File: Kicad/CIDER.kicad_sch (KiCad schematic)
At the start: 0 parts

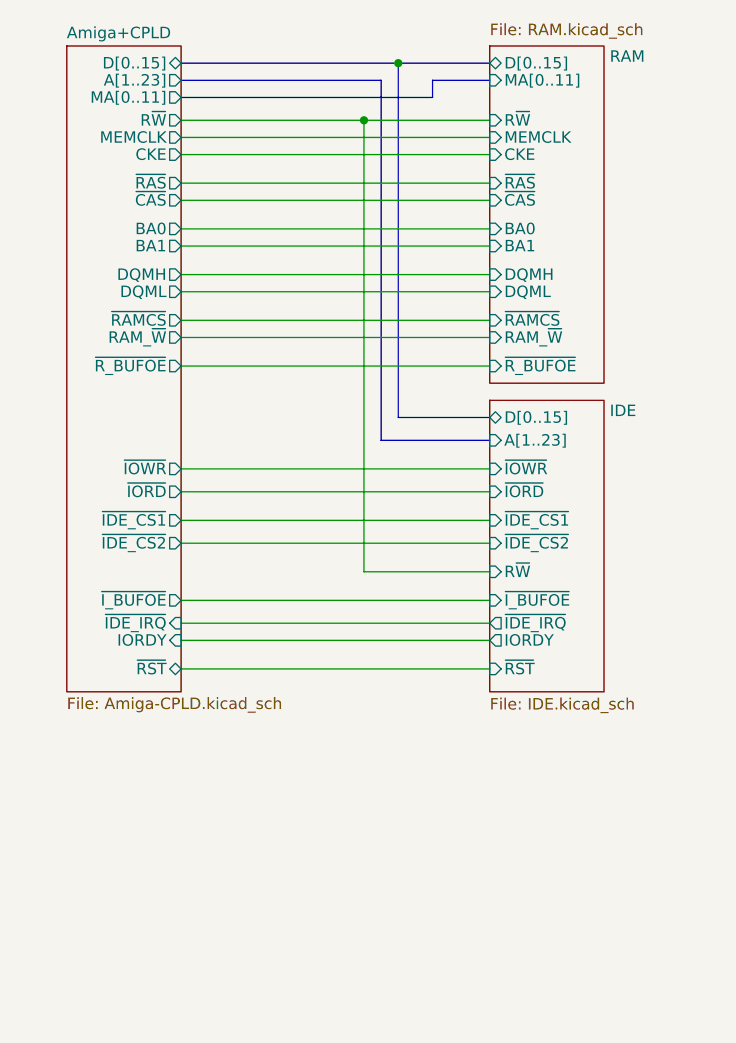
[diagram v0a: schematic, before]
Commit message: PCB: Add 39SF010 for IDE ROM
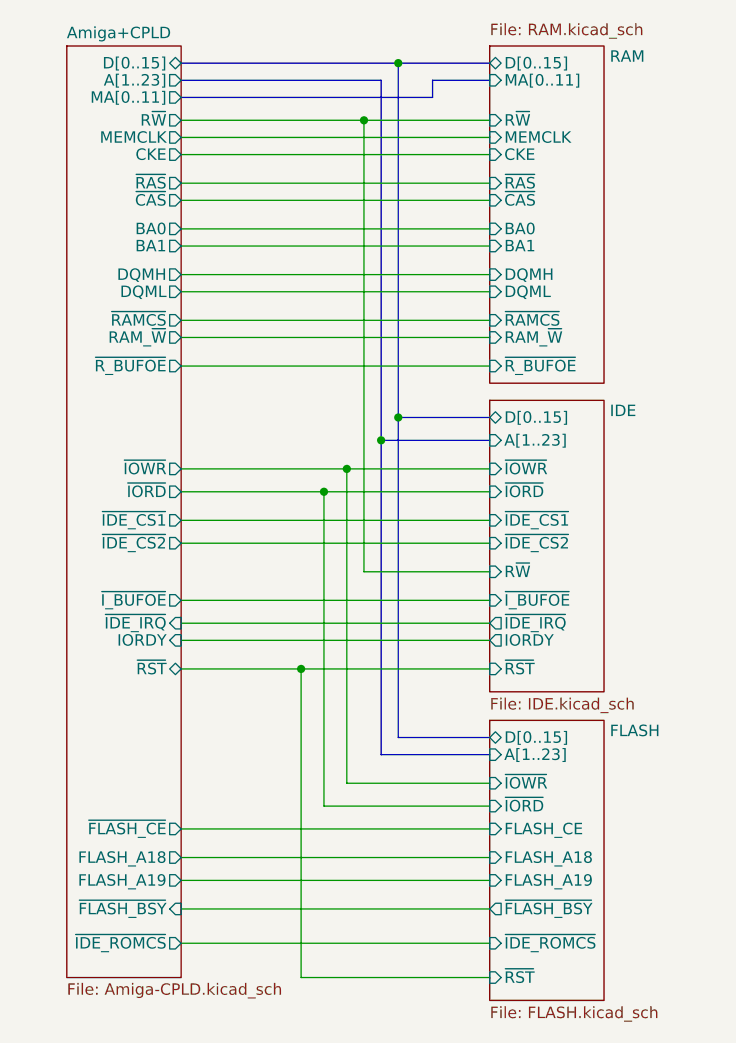
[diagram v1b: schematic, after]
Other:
- added sheet FLASH (FLASH.kicad_sch)
- sheet Amiga+CPLD ports: added FLASH_A18, FLASH_A19, ~{FLASH_BSY}, ~{FLASH_CE}, ~{IDE_ROMCS}; removed none

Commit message: PCB: Keep on routing...
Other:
- sheet Amiga+CPLD ports: added none; removed FLASH_A18, ~{FLASH_BSY}, ~{IDE_IRQ}
- sheet FLASH ports: added none; removed FLASH_A18, ~{FLASH_BSY}
- sheet IDE ports: added none; removed ~{IDE_IRQ}
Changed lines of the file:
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@@
-    (stroke (width 0) (type default) (color 0 0 0 0))
-  )
-  (wire (pts (xy 133.985 121.285) (xy 168.275 121.285))
     (stroke (width 0) (type default) (color 0 0 0 0))
   )
@@
     (stroke (width 0) (type default) (color 0 0 0 0))
   )
-  (wire (pts (xy 133.985 147.32) (xy 168.275 147.32))
-    (stroke (width 0) (type default) (color 0 0 0 0))
-  )
   (bus (pts (xy 156.21 60.96) (xy 156.21 100.965))
     (stroke (width 0) (type default) (color 0 0 0 0))
@@
   )
   (bus (pts (xy 133.985 62.865) (xy 161.925 62.865))
-    (stroke (width 0) (type default) (color 0 0 0 0))
-  )
-  (wire (pts (xy 133.985 153.035) (xy 168.275 153.035))
     (stroke (width 0) (type default) (color 0 0 0 0))
   )
@@
       (effects (font (size 1.27 1.27)) (justify left))
     )
-    (pin "~{IDE_IRQ}" output (at 168.275 121.285 180)
-      (effects (font (size 1.27 1.27)) (justify left))
-    )
     (pin "D[0..15]" bidirectional (at 168.275 98.425 180)
       (effects (font (size 1.27 1.27)) (justify left))
@@
       (effects (font (size 1.27 1.27)) (justify right))
     )
-    (pin "~{IDE_IRQ}" input (at 133.985 121.285 0)
-      (effects (font (size 1.27 1.27)) (justify right))
-    )
     (pin "CKE" output (at 133.985 69.215 0)
       (effects (font (size 1.27 1.27)) (justify right))
@@
       (effects (font (size 1.27 1.27)) (justify right))
     )
-    (pin "FLASH_A18" output (at 133.985 147.32 0)
-      (effects (font (size 1.27 1.27)) (justify right))
-    )
     (pin "FLASH_A19" output (at 133.985 149.86 0)
-      (effects (font (size 1.27 1.27)) (justify right))
-    )
-    (pin "~{FLASH_BSY}" input (at 133.985 153.035 0)
       (effects (font (size 1.27 1.27)) (justify right))
     )
@@
       (effects (font (size 1.27 1.27)) (justify left))
     )
-    (pin "~{FLASH_BSY}" output (at 168.275 153.035 180)
-      (effects (font (size 1.27 1.27)) (justify left))
-    )
     (pin "A[1..23]" input (at 168.275 135.89 180)
       (effects (font (size 1.27 1.27)) (justify left))
     )
-    (pin "FLASH_A18" input (at 168.275 147.32 180)
-      (effects (font (size 1.27 1.27)) (justify left))
-    )

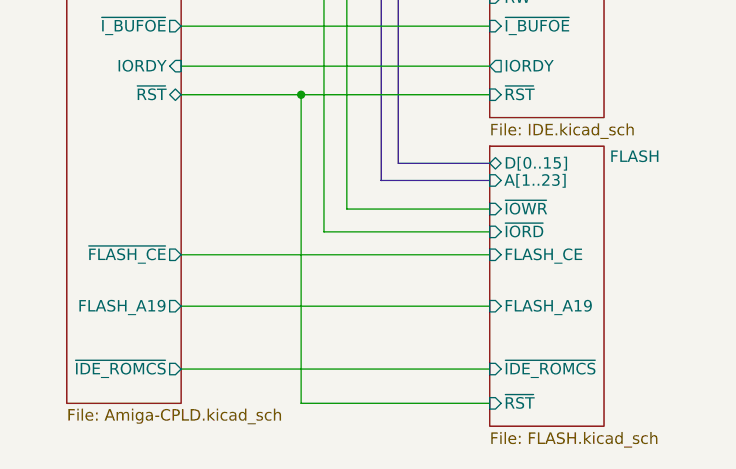
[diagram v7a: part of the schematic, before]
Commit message: PCB: Connect Flash A18 to CPLD
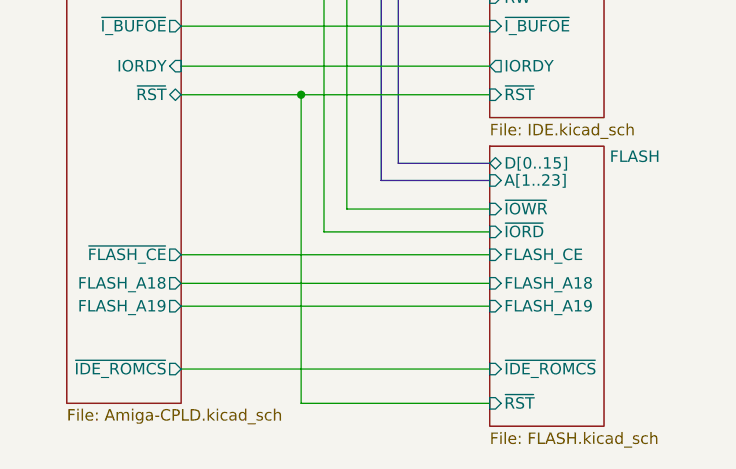
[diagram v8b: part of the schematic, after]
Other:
- sheet Amiga+CPLD ports: added FLASH_A18; removed none
- sheet FLASH ports: added FLASH_A18; removed none
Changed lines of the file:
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@@
+    (stroke (width 0) (type default) (color 0 0 0 0))
+  )
+  (wire (pts (xy 133.985 147.32) (xy 168.275 147.32))
     (stroke (width 0) (type default) (color 0 0 0 0))
   )
@@
       (effects (font (size 1.27 1.27)) (justify right))
     )
+    (pin "FLASH_A18" output (at 133.985 147.32 0)
+      (effects (font (size 1.27 1.27)) (justify right))
+    )
   )
   (sheet (at 168.275 132.08) (size 12.7 31.115)
@@
       (effects (font (size 1.27 1.27)) (justify left))
     )
+    (pin "FLASH_A18" input (at 168.275 147.32 180)
+      (effects (font (size 1.27 1.27)) (justify left))
+    )
